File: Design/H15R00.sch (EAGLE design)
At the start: 36 parts, among them P1 HEXABIT_17.32_NO_P3_P6, U1 STM32F091CBU6, U2 OPA188, X1 XTALL_CSTCE8M00G52

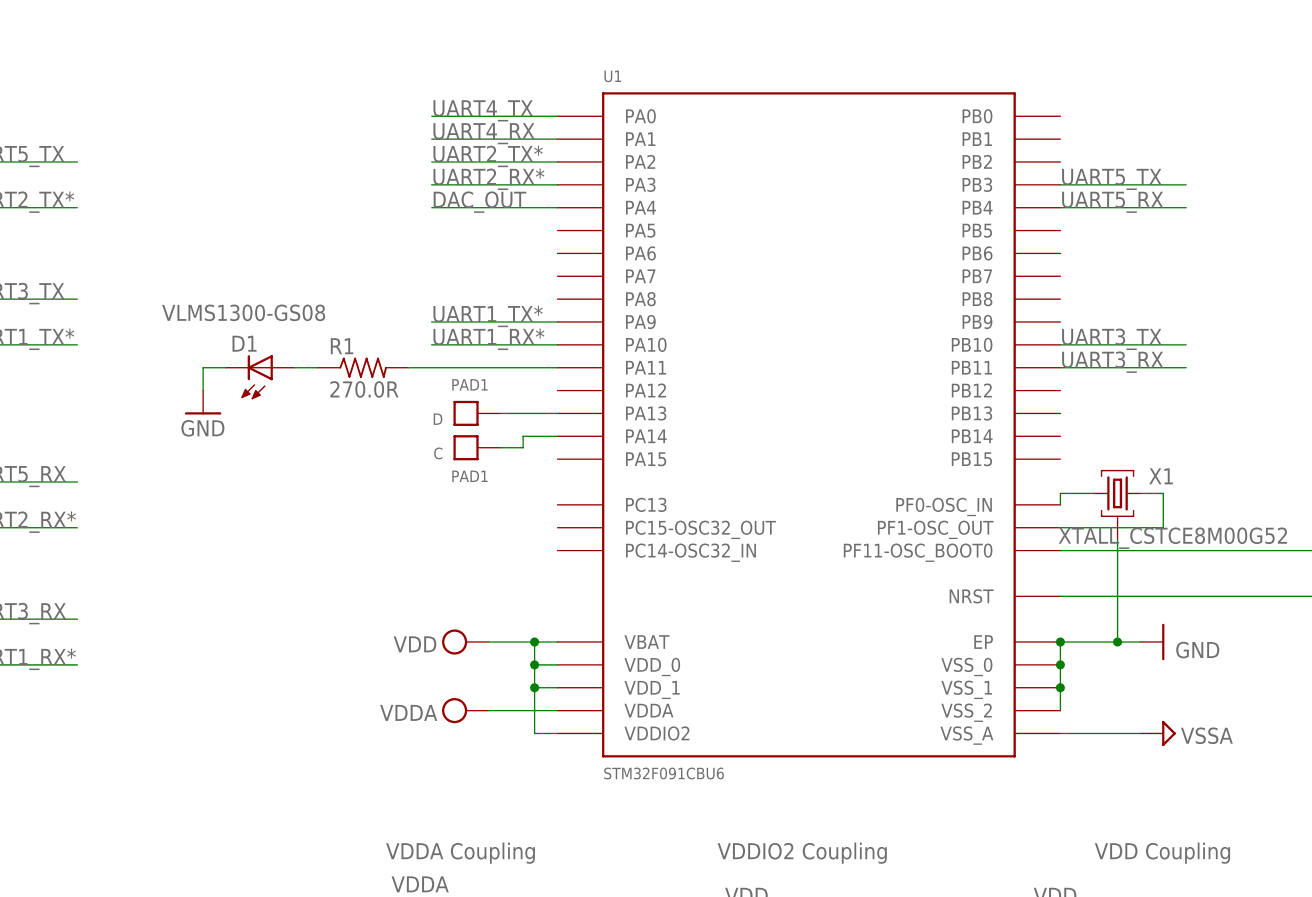
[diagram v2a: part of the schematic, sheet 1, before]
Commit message: Finished routing and silkscreen
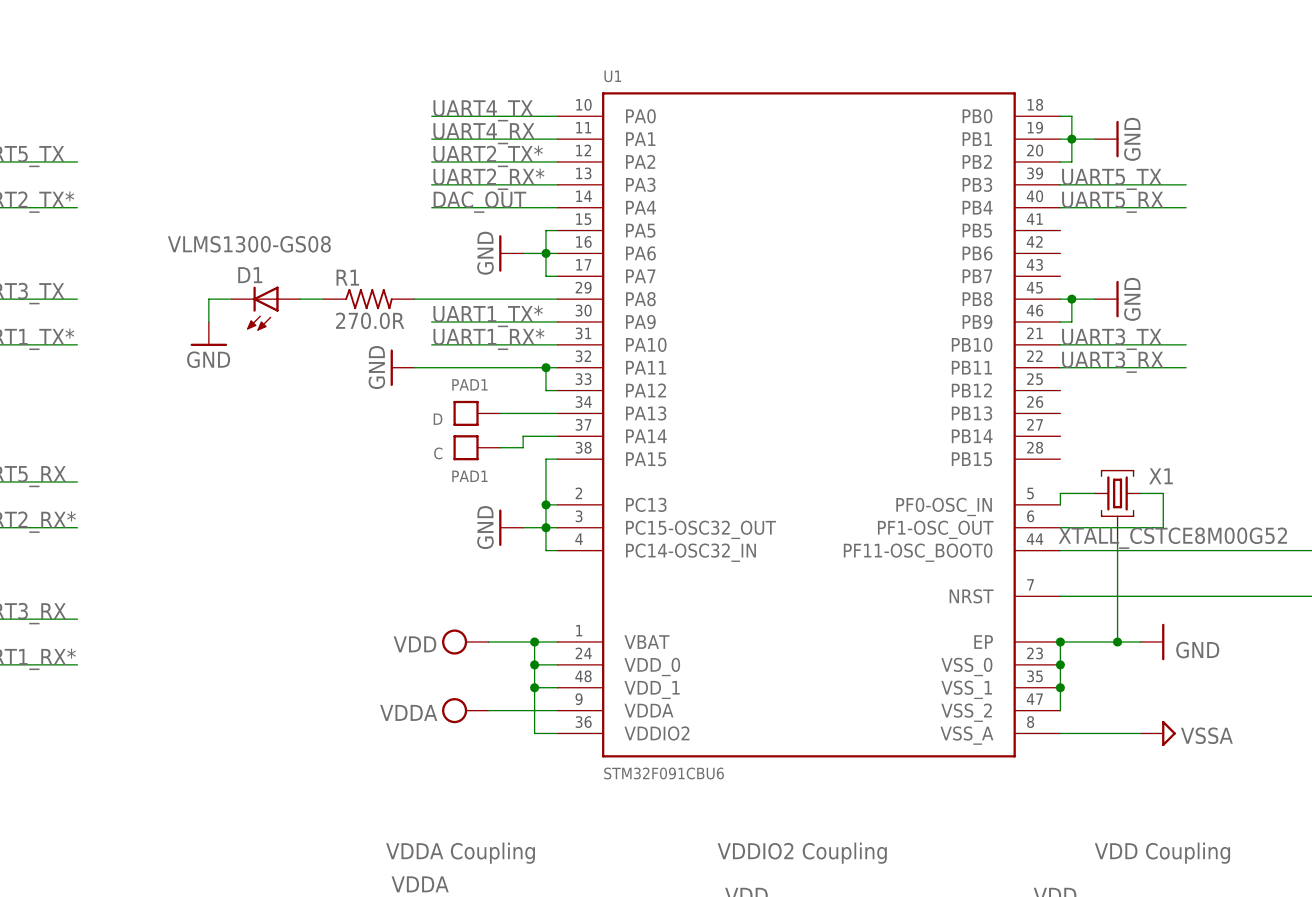
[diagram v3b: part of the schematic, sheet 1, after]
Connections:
- net GND: now also U1.PA11, U1.PA12, U1.PA15, U1.PA5, U1.PA6, U1.PA7, U1.PB0, U1.PB1, U1.PB2, U1.PB8, U1.PB9, U1.PC13, U1.PC14-OSC32_IN, U1.PC15-OSC32_OUT
- net N$3: now also U1.PA8; no longer U1.PA11
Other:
- moved on the sheet: D1, R1
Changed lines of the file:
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@@
 <attribute name="VOLTAGE_RATING" value="50V"/>
 </part>
+<part name="GND9" library="supply1" deviceset="GND" device=""/>
+<part name="GND10" library="supply1" deviceset="GND" device=""/>
+<part name="GND11" library="supply1" deviceset="GND" device=""/>
+<part name="GND12" library="supply1" deviceset="GND" device=""/>
+<part name="GND13" library="supply1" deviceset="GND" device=""/>
 </parts>
 <sheets>
@@
 <attribute name="VALUE" x="156.21" y="58.42" size="1.778" layer="96" rot="R180"/>
 </instance>
-<instance part="R1" gate="G$1" x="114.3" y="149.86" smashed="yes">
-<attribute name="NAME" x="110.49" y="151.3586" size="1.778" layer="95"/>
-<attribute name="VALUE" x="110.49" y="146.558" size="1.778" layer="96"/>
+<instance part="R1" gate="G$1" x="114.935" y="157.48" smashed="yes">
+<attribute name="NAME" x="111.125" y="158.9786" size="1.778" layer="95"/>
+<attribute name="VALUE" x="111.125" y="154.178" size="1.778" layer="96"/>
 </instance>
 <instance part="U1" gate="G$1" x="163.83" y="144.78" smashed="yes">
@@
 <attribute name="VALUE" x="140.97" y="104.14" size="1.27" layer="95"/>
 </instance>
-<instance part="D1" gate="G$1" x="104.14" y="149.86" smashed="yes" rot="MR180">
-<attribute name="NAME" x="99.568" y="153.416" size="1.778" layer="95" rot="MR180"/>
-<attribute name="VALUE" x="91.948" y="156.845" size="1.778" layer="96" rot="MR180"/>
+<instance part="D1" gate="G$1" x="104.775" y="157.48" smashed="yes" rot="MR180">
+<attribute name="NAME" x="100.203" y="161.036" size="1.778" layer="95" rot="MR180"/>
+<attribute name="VALUE" x="92.583" y="164.465" size="1.778" layer="96" rot="MR180"/>
 </instance>
 <instance part="X1" gate="G$1" x="198.12" y="135.89" smashed="yes">
@@
 <attribute name="VALUE" x="217.17" y="132.08" size="1.778" layer="96" rot="R180"/>
 </instance>
-<instance part="GND1" gate="1" x="96.52" y="144.78" smashed="yes">
-<attribute name="VALUE" x="93.98" y="142.24" size="1.778" layer="96"/>
+<instance part="GND1" gate="1" x="97.155" y="152.4" smashed="yes">
+<attribute name="VALUE" x="94.615" y="149.86" size="1.778" layer="96"/>
 </instance>
 <instance part="SUPPLY5" gate="G$1" x="125.73" y="119.38" smashed="yes" rot="R90">
@@
 <instance part="SUPPLY2" gate="GND" x="45.72" y="101.6" smashed="yes">
 <attribute name="VALUE" x="43.815" y="98.425" size="1.778" layer="96"/>
+</instance>
+<instance part="GND9" gate="1" x="117.475" y="149.86" smashed="yes" rot="R270">
+<attribute name="VALUE" x="114.935" y="152.4" size="1.778" layer="96" rot="R270"/>
+</instance>
+<instance part="GND10" gate="1" x="129.54" y="162.56" smashed="yes" rot="R270">
+<attribute name="VALUE" x="127" y="165.1" size="1.778" layer="96" rot="R270"/>
+</instance>
+<instance part="GND11" gate="1" x="198.12" y="175.26" smashed="yes" rot="R90">
+<attribute name="VALUE" x="200.66" y="172.72" size="1.778" layer="96" rot="R90"/>
+</instance>
+<instance part="GND12" gate="1" x="198.12" y="157.48" smashed="yes" rot="R90">
+<attribute name="VALUE" x="200.66" y="154.94" size="1.778" layer="96" rot="R90"/>
+</instance>
+<instance part="GND13" gate="1" x="129.54" y="132.08" smashed="yes" rot="R270">
+<attribute name="VALUE" x="127" y="134.62" size="1.778" layer="96" rot="R270"/>
 </instance>
 </instances>
@@
 <segment>
 <pinref part="GND1" gate="1" pin="GND"/>
-<wire x1="96.52" y1="147.32" x2="96.52" y2="149.86" width="0.1524" layer="91"/>
+<wire x1="97.155" y1="154.94" x2="97.155" y2="157.48" width="0.1524" layer="91"/>
 <pinref part="D1" gate="G$1" pin="C"/>
-<wire x1="96.52" y1="149.86" x2="99.06" y2="149.86" width="0.1524" layer="91"/>
+<wire x1="97.155" y1="157.48" x2="99.695" y2="157.48" width="0.1524" layer="91"/>
 </segment>
 <segment>
@@
 <junction x="45.72" y="111.76"/>
 </segment>
+<segment>
+<pinref part="GND9" gate="1" pin="GND"/>
+<pinref part="U1" gate="G$1" pin="PA11"/>
+<wire x1="120.015" y1="149.86" x2="134.62" y2="149.86" width="0.1524" layer="91"/>
+<pinref part="U1" gate="G$1" pin="PA12"/>
+<wire x1="134.62" y1="149.86" x2="135.89" y2="149.86" width="0.1524" layer="91"/>
+<wire x1="135.89" y1="147.32" x2="134.62" y2="147.32" width="0.1524" layer="91"/>
+<wire x1="134.62" y1="147.32" x2="134.62" y2="149.86" width="0.1524" layer="91"/>
+<junction x="134.62" y="149.86"/>
+</segment>
+<segment>
+<pinref part="GND10" gate="1" pin="GND"/>
+<pinref part="U1" gate="G$1" pin="PA6"/>
+<wire x1="132.08" y1="162.56" x2="134.62" y2="162.56" width="0.1524" layer="91"/>
+<pinref part="U1" gate="G$1" pin="PA5"/>
+<wire x1="134.62" y1="162.56" x2="135.89" y2="162.56" width="0.1524" layer="91"/>
+<wire x1="135.89" y1="165.1" x2="134.62" y2="165.1" width="0.1524" layer="91"/>
+<wire x1="134.62" y1="165.1" x2="134.62" y2="162.56" width="0.1524" layer="91"/>
+<junction x="134.62" y="162.56"/>
+<pinref part="U1" gate="G$1" pin="PA7"/>
+<wire x1="134.62" y1="162.56" x2="134.62" y2="160.02" width="0.1524" layer="91"/>
+<wire x1="134.62" y1="160.02" x2="135.89" y2="160.02" width="0.1524" layer="91"/>
+</segment>
+<segment>
+<pinref part="U1" gate="G$1" pin="PB1"/>
+<pinref part="GND11" gate="1" pin="GND"/>
+<wire x1="191.77" y1="175.26" x2="193.04" y2="175.26" width="0.1524" layer="91"/>
+<pinref part="U1" gate="G$1" pin="PB2"/>
+<wire x1="193.04" y1="175.26" x2="195.58" y2="175.26" width="0.1524" layer="91"/>
+<wire x1="191.77" y1="172.72" x2="193.04" y2="172.72" width="0.1524" layer="91"/>
+<wire x1="193.04" y1="172.72" x2="193.04" y2="175.26" width="0.1524" layer="91"/>
+<junction x="193.04" y="175.26"/>
+<pinref part="U1" gate="G$1" pin="PB0"/>
+<wire x1="191.77" y1="177.8" x2="193.04" y2="177.8" width="0.1524" layer="91"/>
+<wire x1="193.04" y1="177.8" x2="193.04" y2="175.26" width="0.1524" layer="91"/>
+</segment>
+<segment>
+<pinref part="GND12" gate="1" pin="GND"/>
+<pinref part="U1" gate="G$1" pin="PB8"/>
+<wire x1="195.58" y1="157.48" x2="193.04" y2="157.48" width="0.1524" layer="91"/>
+<pinref part="U1" gate="G$1" pin="PB9"/>
+<wire x1="193.04" y1="157.48" x2="191.77" y2="157.48" width="0.1524" layer="91"/>
+<wire x1="191.77" y1="154.94" x2="193.04" y2="154.94" width="0.1524" layer="91"/>
+<wire x1="193.04" y1="154.94" x2="193.04" y2="157.48" width="0.1524" layer="91"/>
+<junction x="193.04" y="157.48"/>
+</segment>
+<segment>
+<pinref part="U1" gate="G$1" pin="PA15"/>
+<pinref part="GND13" gate="1" pin="GND"/>
+<wire x1="135.89" y1="139.7" x2="134.62" y2="139.7" width="0.1524" layer="91"/>
+<wire x1="134.62" y1="139.7" x2="134.62" y2="134.62" width="0.1524" layer="91"/>
+<wire x1="134.62" y1="134.62" x2="134.62" y2="132.08" width="0.1524" layer="91"/>
+<wire x1="134.62" y1="132.08" x2="132.08" y2="132.08" width="0.1524" layer="91"/>
+<pinref part="U1" gate="G$1" pin="PC14-OSC32_IN"/>
+<wire x1="135.89" y1="129.54" x2="134.62" y2="129.54" width="0.1524" layer="91"/>
+<wire x1="134.62" y1="129.54" x2="134.62" y2="132.08" width="0.1524" layer="91"/>
+<junction x="134.62" y="132.08"/>
+<pinref part="U1" gate="G$1" pin="PC15-OSC32_OUT"/>
+<wire x1="135.89" y1="132.08" x2="134.62" y2="132.08" width="0.1524" layer="91"/>
+<pinref part="U1" gate="G$1" pin="PC13"/>
+<wire x1="135.89" y1="134.62" x2="134.62" y2="134.62" width="0.1524" layer="91"/>
+<junction x="134.62" y="134.62"/>
+</segment>
 </net>
 <net name="UART5_TX" class="0">
@@
 <net name="N$3" class="0">
 <segment>
-<pinref part="U1" gate="G$1" pin="PA11"/>
+<pinref part="U1" gate="G$1" pin="PA8"/>
+<wire x1="135.89" y1="157.48" x2="120.015" y2="157.48" width="0.1524" layer="91"/>
 <pinref part="R1" gate="G$1" pin="2"/>
-<wire x1="135.89" y1="149.86" x2="119.38" y2="149.86" width="0.1524" layer="91"/>
 </segment>
 </net>
@@
 <pinref part="R1" gate="G$1" pin="1"/>
 <pinref part="D1" gate="G$1" pin="A"/>
-<wire x1="109.22" y1="149.86" x2="106.68" y2="149.86" width="0.1524" layer="91"/>
+<wire x1="109.855" y1="157.48" x2="107.315" y2="157.48" width="0.1524" layer="91"/>
 </segment>
 </net>

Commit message: Solved DRC Generated gerber, drill, pick n place and schematics Generated BOM First release Ver 0
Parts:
- R7: RESISTANCE 12.4 Ohm -> 12.4 kOhm
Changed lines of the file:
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@@
 <attribute name="MPN" value="ERA-3AEB1242V"/>
 <attribute name="OCTOPART_URL" value="https://octopart.com/era-3aeb1242v-panasonic-55639351?r=sp&amp;s=K0xQjqOwSGaT1tqbXnh0hg"/>
-<attribute name="RESISTANCE" value="12.4 Ohm"/>
+<attribute name="RESISTANCE" value="12.4 kOhm"/>
 <attribute name="TOLERANCE" value="0.1%"/>
 </part>
